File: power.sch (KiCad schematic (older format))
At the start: 15 parts

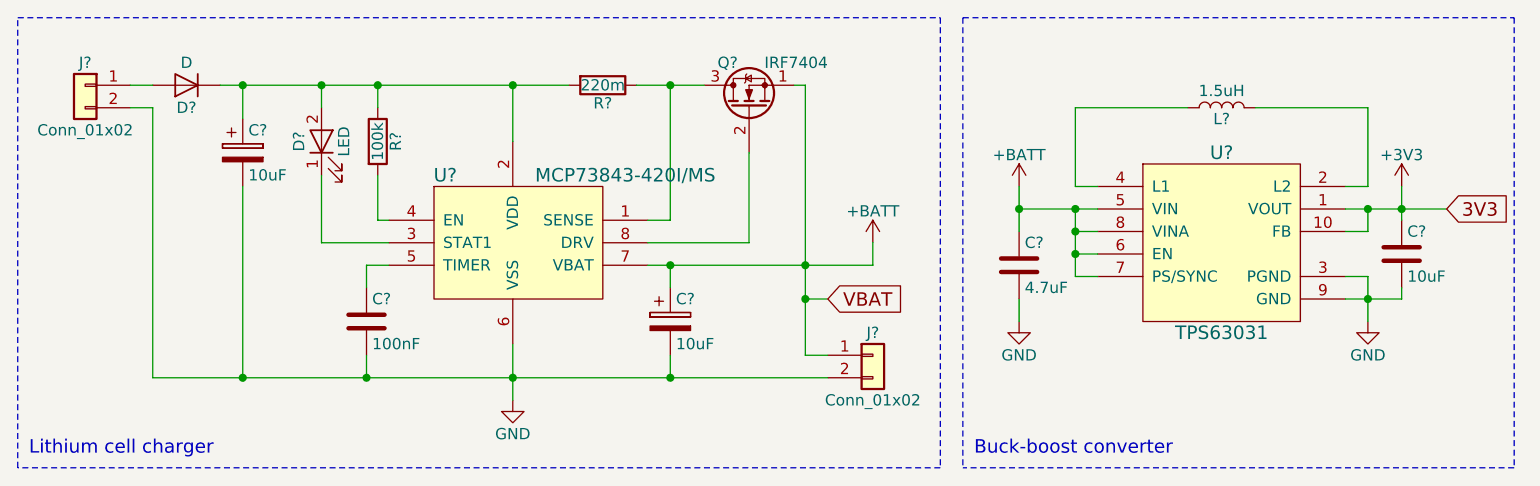
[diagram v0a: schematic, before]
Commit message: Remove redundant global power labels
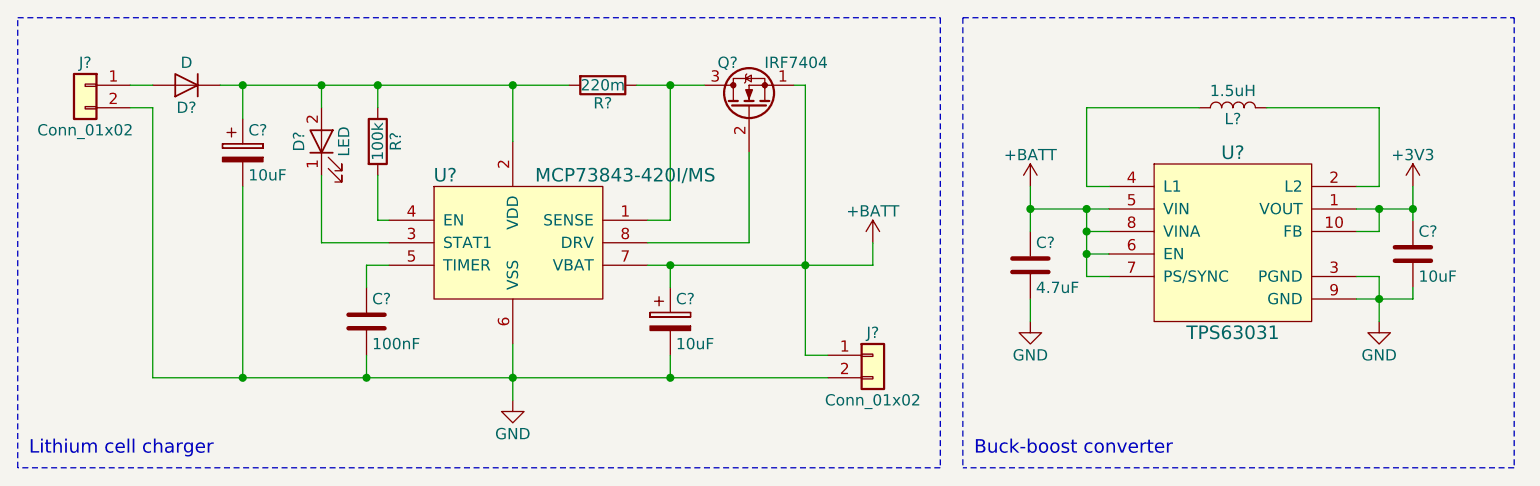
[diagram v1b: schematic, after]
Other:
- moved on the sheet: C?, L?, U?
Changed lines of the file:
@@
 L TPS63031 U?
 U 1 1 5A6FBC59
-P 6650 1950
-F 0 "U?" H 6650 2350 60  0000 C CNN
-F 1 "TPS63031" H 6650 1550 60  0000 C CNN
-F 2 "" H 6650 1450 60  0001 C CNN
-F 3 "" H 6650 1450 60  0001 C CNN
-	1    6650 1950
+P 6700 1950
+F 0 "U?" H 6700 2350 60  0000 C CNN
+F 1 "TPS63031" H 6700 1550 60  0000 C CNN
+F 2 "" H 6700 1450 60  0001 C CNN
+F 3 "" H 6700 1450 60  0001 C CNN
+	1    6700 1950
 	1    0    0    -1
 $EndComp
@@
 L L L?
 U 1 1 5A6FBD77
-P 6650 1350
-F 0 "L?" V 6600 1350 50  0000 C CNN
-F 1 "1.5uH" V 6725 1350 50  0000 C CNN
-F 2 "" H 6650 1350 50  0001 C CNN
-F 3 "" H 6650 1350 50  0001 C CNN
-	1    6650 1350
+P 6700 1350
+F 0 "L?" V 6650 1350 50  0000 C CNN
+F 1 "1.5uH" V 6775 1350 50  0000 C CNN
+F 2 "" H 6700 1350 50  0001 C CNN
+F 3 "" H 6700 1350 50  0001 C CNN
+	1    6700 1350
 	0    -1   -1   0
 $EndComp
 Wire Wire Line
-	6000 1350 6000 1700
+	6050 1350 6050 1700
 Wire Wire Line
-	6000 1700 6100 1700
+	6050 1700 6150 1700
 Wire Wire Line
-	7300 1350 7300 1700
+	7350 1350 7350 1700
 Wire Wire Line
-	7300 1700 7200 1700
+	7350 1700 7250 1700
 Wire Wire Line
-	7300 1350 6800 1350
+	7350 1350 6850 1350
 Wire Wire Line
-	6500 1350 6000 1350
+	6550 1350 6050 1350
 $Comp
 L C C?
 U 1 1 5A6FC08C
-P 5750 2050
-F 0 "C?" H 5775 2150 50  0000 L CNN
-F 1 "4.7uF" H 5775 1950 50  0000 L CNN
-F 2 "" H 5788 1900 50  0001 C CNN
-F 3 "" H 5750 2050 50  0001 C CNN
-	1    5750 2050
+P 5800 2050
+F 0 "C?" H 5825 2150 50  0000 L CNN
+F 1 "4.7uF" H 5825 1950 50  0000 L CNN
+F 2 "" H 5838 1900 50  0001 C CNN
+F 3 "" H 5800 2050 50  0001 C CNN
+	1    5800 2050
 	1    0    0    -1
 $EndComp
@@
 L C C?
 U 1 1 5A6FC1B6
-P 7450 2000
-F 0 "C?" H 7475 2100 50  0000 L CNN
-F 1 "10uF" H 7475 1900 50  0000 L CNN
-F 2 "" H 7488 1850 50  0001 C CNN
-F 3 "" H 7450 2000 50  0001 C CNN
-	1    7450 2000
+P 7500 2000
+F 0 "C?" H 7525 2100 50  0000 L CNN
+F 1 "10uF" H 7525 1900 50  0000 L CNN
+F 2 "" H 7538 1850 50  0001 C CNN
+F 3 "" H 7500 2000 50  0001 C CNN
+	1    7500 2000
 	1    0    0    -1
 $EndComp
 Wire Wire Line
-	5750 1700 5750 1900
+	5800 1700 5800 1900
 Wire Wire Line
-	6100 1900 6000 1900
+	6150 1900 6050 1900
 Wire Wire Line
-	6000 1800 6000 2100
-Connection ~ 6000 1800
+	6050 1800 6050 2100
+Connection ~ 6050 1800
 Wire Wire Line
-	6000 2000 6100 2000
-Connection ~ 6000 1900
+	6050 2000 6150 2000
+Connection ~ 6050 1900
 Wire Wire Line
-	6000 2100 6100 2100
-Connection ~ 6000 2000
+	6050 2100 6150 2100
+Connection ~ 6050 2000
 $Comp
 L GND #PWR?
 U 1 1 5A6FC3F5
-P 5750 2300
-F 0 "#PWR?" H 5750 2050 50  0001 C CNN
-F 1 "GND" H 5750 2150 50  0000 C CNN
-F 2 "" H 5750 2300 50  0001 C CNN
-F 3 "" H 5750 2300 50  0001 C CNN
-	1    5750 2300
+P 5800 2300
+F 0 "#PWR?" H 5800 2050 50  0001 C CNN
+F 1 "GND" H 5800 2150 50  0000 C CNN
+F 2 "" H 5800 2300 50  0001 C CNN
+F 3 "" H 5800 2300 50  0001 C CNN
+	1    5800 2300
 	1    0    0    -1
 $EndComp
 Wire Wire Line
-	5750 2200 5750 2300
+	5800 2200 5800 2300
 $Comp
 L GND #PWR?
 U 1 1 5A6FC483
-P 7300 2300
-F 0 "#PWR?" H 7300 2050 50  0001 C CNN
-F 1 "GND" H 7300 2150 50  0000 C CNN
-F 2 "" H 7300 2300 50  0001 C CNN
-F 3 "" H 7300 2300 50  0001 C CNN
-	1    7300 2300
+P 7350 2300
+F 0 "#PWR?" H 7350 2050 50  0001 C CNN
+F 1 "GND" H 7350 2150 50  0000 C CNN
+F 2 "" H 7350 2300 50  0001 C CNN
+F 3 "" H 7350 2300 50  0001 C CNN
+	1    7350 2300
 	1    0    0    -1
 $EndComp
 Wire Wire Line
-	7200 2100 7300 2100
+	7250 2100 7350 2100
 Wire Wire Line
-	7200 2200 7450 2200
-Connection ~ 7300 2200
+	7250 2200 7500 2200
+Connection ~ 7350 2200
 Wire Wire Line
-	7200 1900 7300 1900
+	7250 1900 7350 1900
 Wire Wire Line
-	7300 1900 7300 1800
-Connection ~ 7300 1800
+	7350 1900 7350 1800
+Connection ~ 7350 1800
 $Comp
 L +BATT #PWR?
 U 1 1 5A6FCC3D
-P 5750 1700
-F 0 "#PWR?" H 5750 1550 50  0001 C CNN
-F 1 "+BATT" H 5750 1840 50  0000 C CNN
-F 2 "" H 5750 1700 50  0001 C CNN
-F 3 "" H 5750 1700 50  0001 C CNN
-	1    5750 1700
+P 5800 1700
+F 0 "#PWR?" H 5800 1550 50  0001 C CNN
+F 1 "+BATT" H 5800 1840 50  0000 C CNN
+F 2 "" H 5800 1700 50  0001 C CNN
+F 3 "" H 5800 1700 50  0001 C CNN
+	1    5800 1700
 	1    0    0    -1
 $EndComp
-Connection ~ 5750 1800
+Connection ~ 5800 1800
 Wire Wire Line
-	5750 1800 6100 1800
+	5800 1800 6150 1800
 Wire Wire Line
-	7200 1800 7650 1800
+	7500 1700 7500 1850
 Wire Wire Line
-	7450 1700 7450 1850
+	7500 2200 7500 2150
 Wire Wire Line
-	7450 2200 7450 2150
-Wire Wire Line
-	7300 2100 7300 2300
-Text GLabel 7650 1800 2    60   Input ~ 0
-3V3
+	7350 2100 7350 2300
 $Comp
 L +3V3 #PWR?
 U 1 1 5A6FDAFA
-P 7450 1700
-F 0 "#PWR?" H 7450 1550 50  0001 C CNN
-F 1 "+3V3" H 7450 1840 50  0000 C CNN
-F 2 "" H 7450 1700 50  0001 C CNN
-F 3 "" H 7450 1700 50  0001 C CNN
-	1    7450 1700
+P 7500 1700
+F 0 "#PWR?" H 7500 1550 50  0001 C CNN
+F 1 "+3V3" H 7500 1840 50  0000 C CNN
+F 2 "" H 7500 1700 50  0001 C CNN
+F 3 "" H 7500 1700 50  0001 C CNN
+	1    7500 1700
 	1    0    0    -1
 $EndComp
-Connection ~ 7450 1800
-Text GLabel 4900 2200 2    60   Input ~ 0
-VBAT
+Connection ~ 7500 1800
 Wire Wire Line
 	4100 2050 5100 2050
@@
 	4800 2450 4900 2450
 Connection ~ 4800 2050
-Wire Wire Line
-	4900 2200 4800 2200
-Connection ~ 4800 2200
 Wire Wire Line
 	4800 1250 4800 2450
@@
 Text Notes 5550 2900 0    60   ~ 0
 Buck-boost converter
+Wire Wire Line
+	7250 1800 7500 1800
 $EndSCHEMATC
